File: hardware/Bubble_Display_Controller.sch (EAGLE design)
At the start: 37 parts, among them J1 ICSP, Q1 BSS84, Q10 BSS123, Q11 BSS123, Q12 BSS123, Q13 BSS123, Q14 BSS123, Q15 BSS123, Q16 BSS123, Q2 BSS84, Q3 BSS84, Q4 BSS84, Q5 BSS84, Q6 BSS84, Q7 BSS84, Q8 BSS84, Q9 BSS123, U4 ATMEGA328, Y1 16MHz

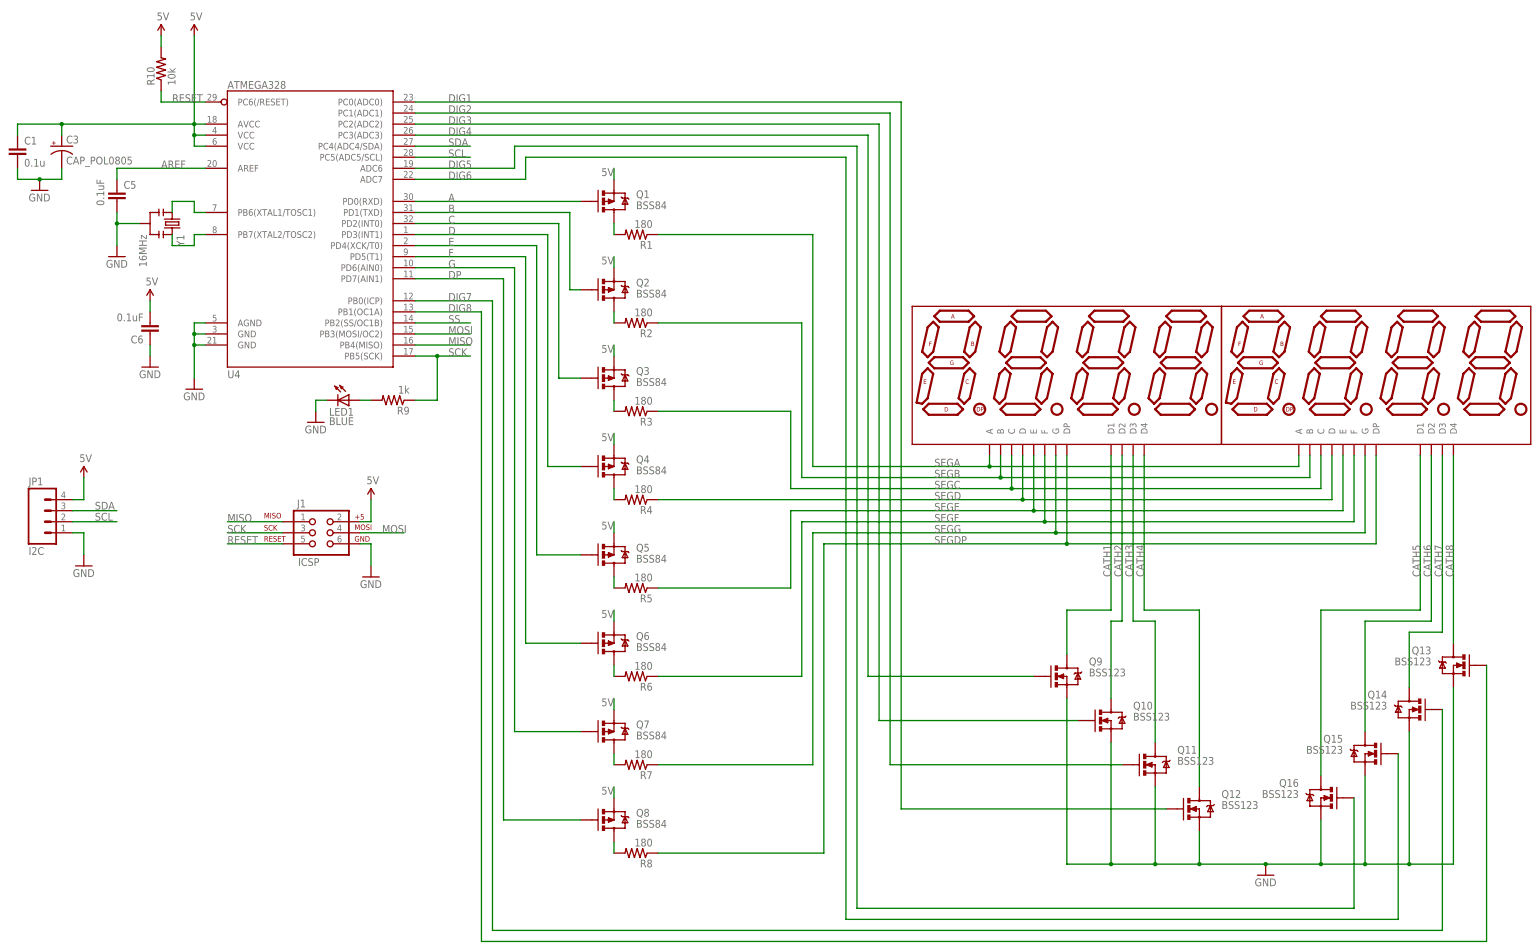
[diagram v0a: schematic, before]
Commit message: Updating comp values per simulation. Added BOM. Started firmware.
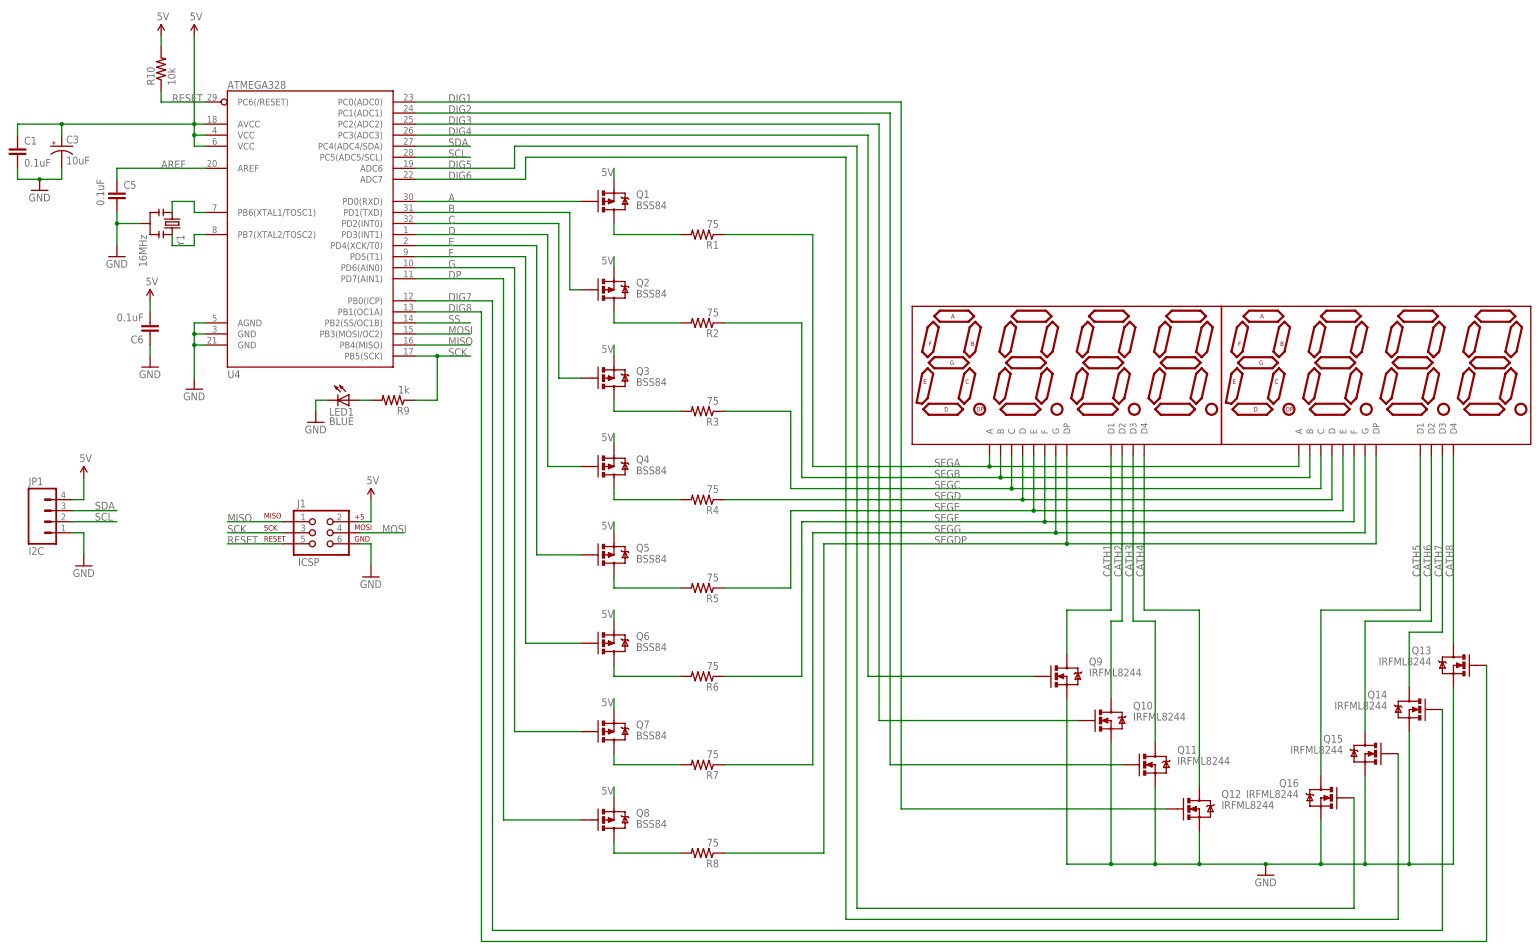
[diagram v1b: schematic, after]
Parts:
- C1: value 0.1u -> 0.1uF
- C3: value CAP_POL0805 -> 10uF
- Q10, Q11, Q12, Q13, Q14, Q15, Q16, Q9: value BSS123 -> IRFML8244
- R1, R2, R3, R4, R5, R6, R7, R8: value 180 -> 75
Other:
- moved on the sheet: R1, R2, R3, R4, R5, R6, R7, R8

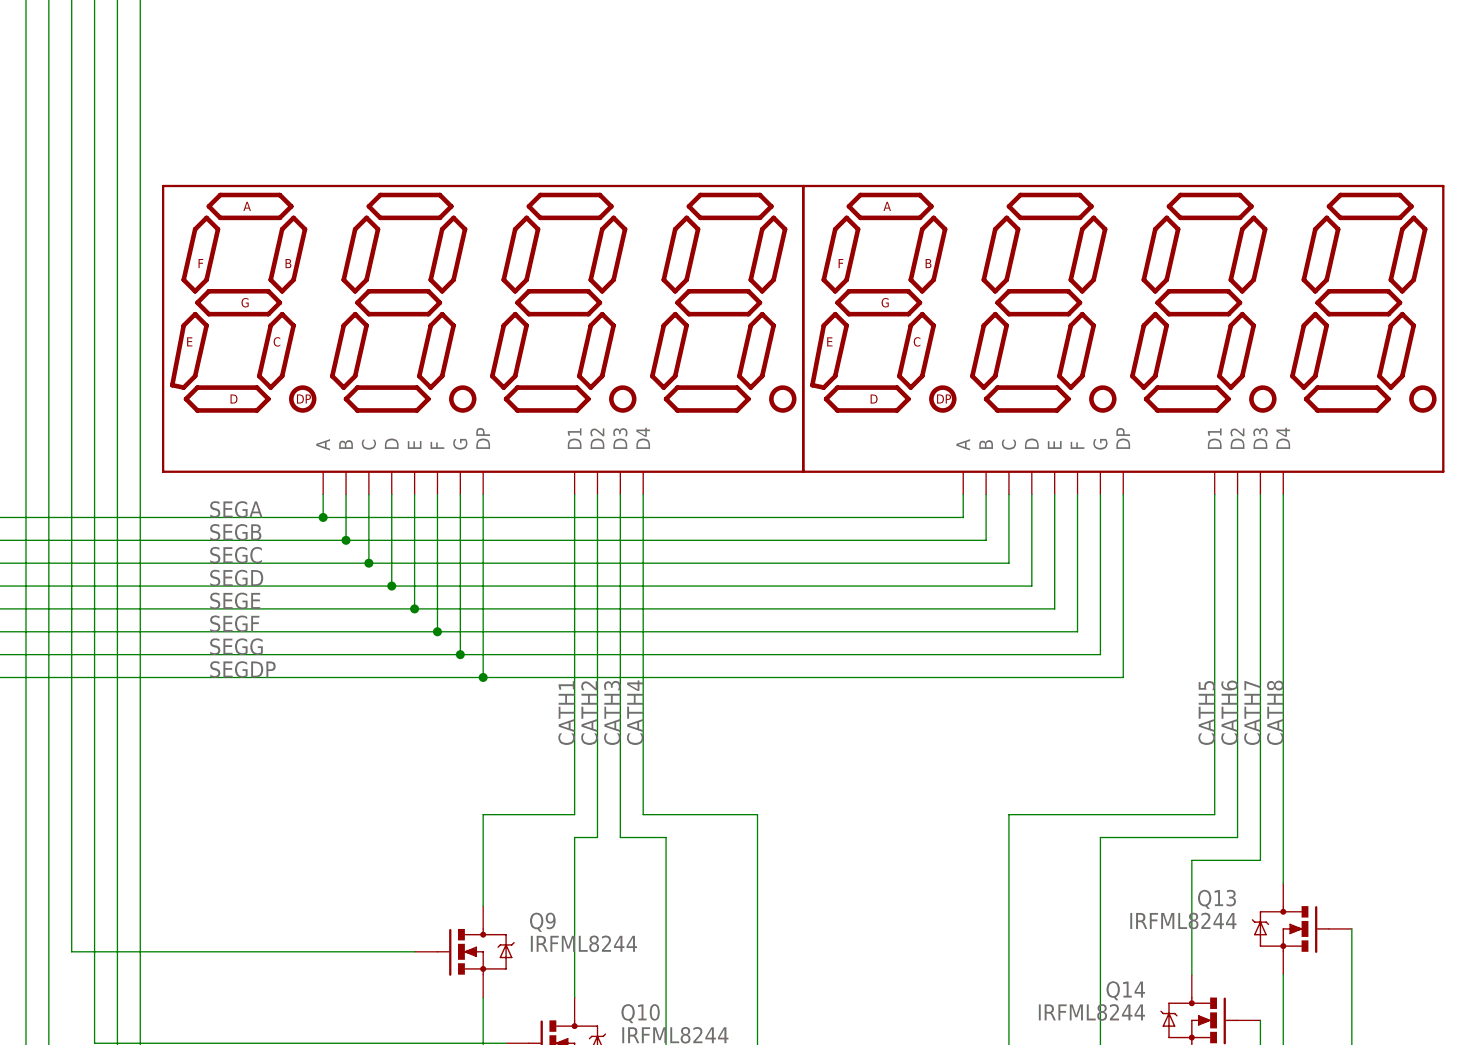
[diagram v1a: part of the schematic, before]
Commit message: Updated to use new HP Display component in my fork of SparkFun libraries
Also worked on CharGenROM.h; converted segments to HP config.  Added
proper port manipulation to Display_Firmware.ino.
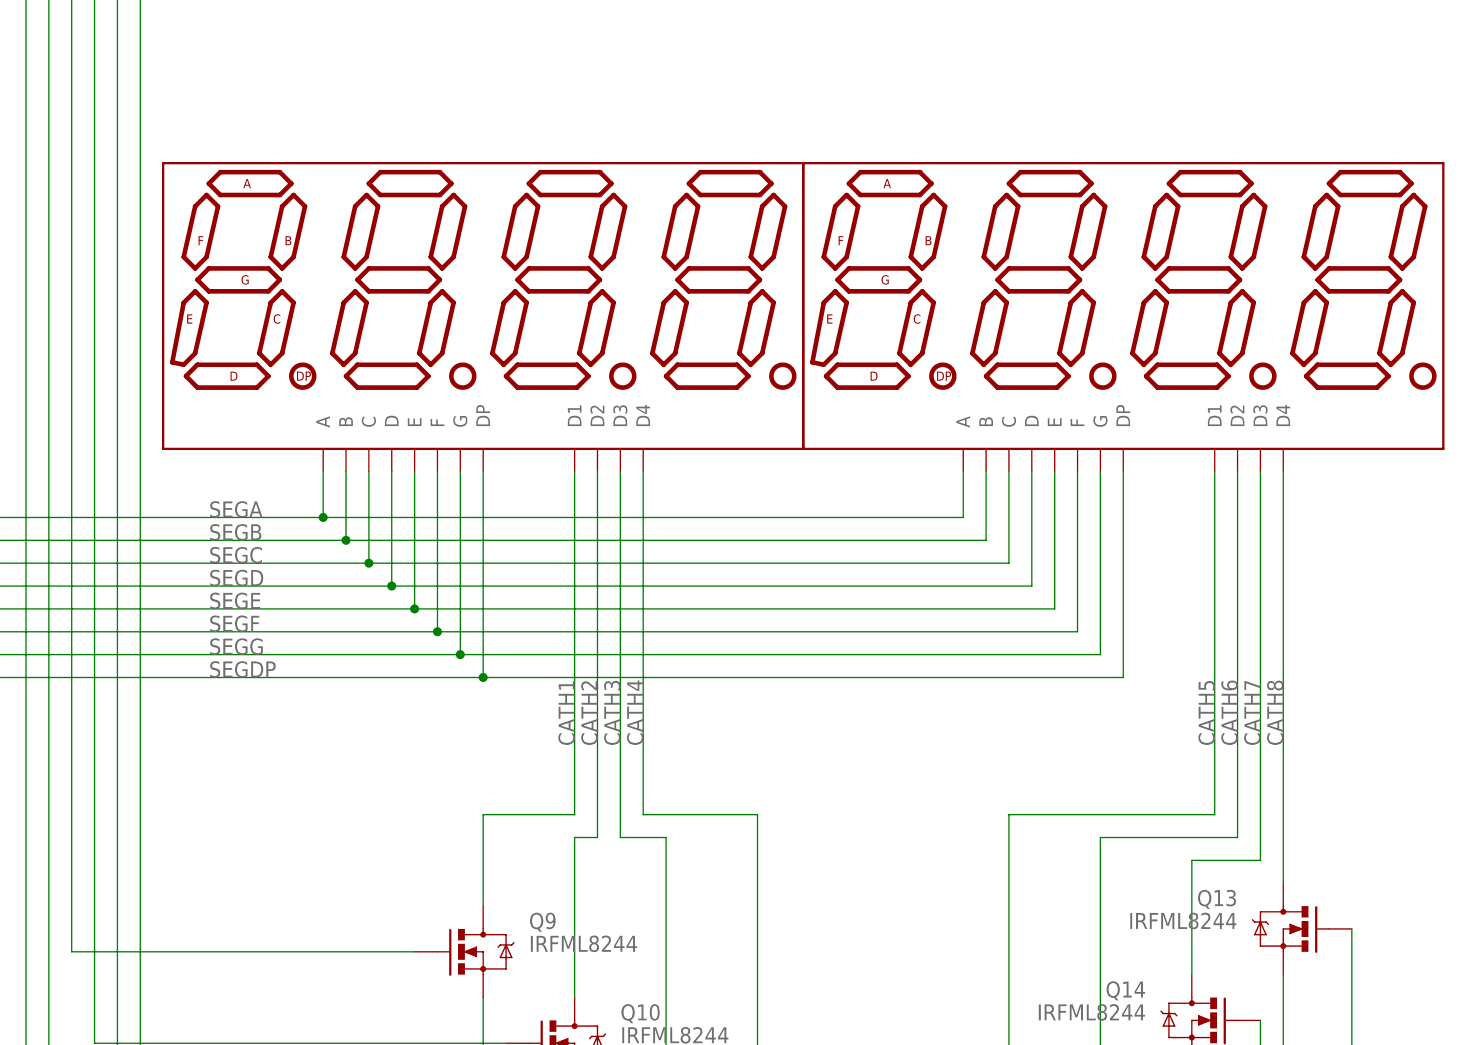
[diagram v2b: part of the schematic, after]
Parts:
- DISPLAY1, DISPLAY2: device SparkFun-Displays:7-SEGMENT-4DIGIT-COUNTER-HP-BUBBLE-DISPLAY -> SparkFun-Displays:7-SEGMENT-4DIGIT-COUNTER-HP-BUBBLE
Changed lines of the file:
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@@
 </classes>
 <parts>
-<part name="DISPLAY1" library="SparkFun-Displays" deviceset="7-SEGMENT-4DIGIT-COUNTER" device="-HP-BUBBLE-DISPLAY" value="hp"/>
-<part name="DISPLAY2" library="SparkFun-Displays" deviceset="7-SEGMENT-4DIGIT-COUNTER" device="-HP-BUBBLE-DISPLAY" value="hp"/>
+<part name="DISPLAY1" library="SparkFun-Displays" deviceset="7-SEGMENT-4DIGIT-COUNTER" device="-HP-BUBBLE" value="hp"/>
+<part name="DISPLAY2" library="SparkFun-Displays" deviceset="7-SEGMENT-4DIGIT-COUNTER" device="-HP-BUBBLE" value="hp"/>
 <part name="Q1" library="SparkFun-DiscreteSemi" deviceset="MOSFET-PCHANNEL" device="SMD" value="BSS84"/>
 <part name="R1" library="SparkFun-Resistors" deviceset="RESISTOR" device="0805-RES" value="75"/>
@@
 </plain>
 <instances>
-<instance part="DISPLAY1" gate="G$1" x="-25.4" y="0"/>
-<instance part="DISPLAY2" gate="G$1" x="45.72" y="0"/>
+<instance part="DISPLAY1" gate="G$1" x="-25.4" y="2.54"/>
+<instance part="DISPLAY2" gate="G$1" x="45.72" y="2.54"/>
 <instance part="Q1" gate="G$1" x="-129.54" y="40.64" smashed="yes" rot="MR180">
 <attribute name="NAME" x="-124.46" y="43.18" size="1.778" layer="95" rot="MR180"/>
@@
 <segment>
 <pinref part="DISPLAY2" gate="G$1" pin="B"/>
-<wire x1="30.48" y1="-17.78" x2="30.48" y2="-22.86" width="0.1524" layer="91"/>
+<wire x1="30.48" y1="-15.24" x2="30.48" y2="-22.86" width="0.1524" layer="91"/>
 <wire x1="30.48" y1="-22.86" x2="-40.64" y2="-22.86" width="0.1524" layer="91"/>
 <pinref part="DISPLAY1" gate="G$1" pin="B"/>
-<wire x1="-40.64" y1="-22.86" x2="-40.64" y2="-17.78" width="0.1524" layer="91"/>
+<wire x1="-40.64" y1="-22.86" x2="-40.64" y2="-15.24" width="0.1524" layer="91"/>
 <wire x1="-40.64" y1="-22.86" x2="-86.36" y2="-22.86" width="0.1524" layer="91"/>
 <wire x1="-86.36" y1="-22.86" x2="-86.36" y2="12.7" width="0.1524" layer="91"/>
@@
 <segment>
 <pinref part="DISPLAY2" gate="G$1" pin="D"/>
-<wire x1="35.56" y1="-17.78" x2="35.56" y2="-27.94" width="0.1524" layer="91"/>
+<wire x1="35.56" y1="-15.24" x2="35.56" y2="-27.94" width="0.1524" layer="91"/>
 <wire x1="35.56" y1="-27.94" x2="-35.56" y2="-27.94" width="0.1524" layer="91"/>
 <pinref part="DISPLAY1" gate="G$1" pin="D"/>
-<wire x1="-35.56" y1="-27.94" x2="-35.56" y2="-17.78" width="0.1524" layer="91"/>
+<wire x1="-35.56" y1="-27.94" x2="-35.56" y2="-15.24" width="0.1524" layer="91"/>
 <wire x1="-35.56" y1="-27.94" x2="-104.14" y2="-27.94" width="0.1524" layer="91"/>
 <pinref part="R4" gate="G$1" pin="1"/>
@@
 <segment>
 <pinref part="DISPLAY2" gate="G$1" pin="E"/>
-<wire x1="38.1" y1="-17.78" x2="38.1" y2="-30.48" width="0.1524" layer="91"/>
+<wire x1="38.1" y1="-15.24" x2="38.1" y2="-30.48" width="0.1524" layer="91"/>
 <wire x1="38.1" y1="-30.48" x2="-33.02" y2="-30.48" width="0.1524" layer="91"/>
 <pinref part="DISPLAY1" gate="G$1" pin="E"/>
-<wire x1="-33.02" y1="-30.48" x2="-33.02" y2="-17.78" width="0.1524" layer="91"/>
+<wire x1="-33.02" y1="-30.48" x2="-33.02" y2="-15.24" width="0.1524" layer="91"/>
 <pinref part="R5" gate="G$1" pin="1"/>
 <wire x1="-88.9" y1="-48.26" x2="-104.14" y2="-48.26" width="0.1524" layer="91"/>
@@
 <segment>
 <pinref part="DISPLAY2" gate="G$1" pin="F"/>
-<wire x1="40.64" y1="-17.78" x2="40.64" y2="-33.02" width="0.1524" layer="91"/>
+<wire x1="40.64" y1="-15.24" x2="40.64" y2="-33.02" width="0.1524" layer="91"/>
 <wire x1="40.64" y1="-33.02" x2="-30.48" y2="-33.02" width="0.1524" layer="91"/>
 <pinref part="DISPLAY1" gate="G$1" pin="F"/>
-<wire x1="-30.48" y1="-33.02" x2="-30.48" y2="-17.78" width="0.1524" layer="91"/>
+<wire x1="-30.48" y1="-33.02" x2="-30.48" y2="-15.24" width="0.1524" layer="91"/>
 <wire x1="-86.36" y1="-68.58" x2="-104.14" y2="-68.58" width="0.1524" layer="91"/>
 <pinref part="R6" gate="G$1" pin="1"/>
@@
 <segment>
 <pinref part="DISPLAY2" gate="G$1" pin="G"/>
-<wire x1="43.18" y1="-17.78" x2="43.18" y2="-35.56" width="0.1524" layer="91"/>
+<wire x1="43.18" y1="-15.24" x2="43.18" y2="-35.56" width="0.1524" layer="91"/>
 <wire x1="43.18" y1="-35.56" x2="-27.94" y2="-35.56" width="0.1524" layer="91"/>
 <pinref part="DISPLAY1" gate="G$1" pin="G"/>
-<wire x1="-27.94" y1="-35.56" x2="-27.94" y2="-17.78" width="0.1524" layer="91"/>
+<wire x1="-27.94" y1="-35.56" x2="-27.94" y2="-15.24" width="0.1524" layer="91"/>
 <wire x1="-27.94" y1="-35.56" x2="-83.82" y2="-35.56" width="0.1524" layer="91"/>
 <wire x1="-83.82" y1="-35.56" x2="-83.82" y2="-88.9" width="0.1524" layer="91"/>
@@
 <segment>
 <pinref part="DISPLAY2" gate="G$1" pin="DP"/>
-<wire x1="45.72" y1="-17.78" x2="45.72" y2="-38.1" width="0.1524" layer="91"/>
+<wire x1="45.72" y1="-15.24" x2="45.72" y2="-38.1" width="0.1524" layer="91"/>
 <wire x1="45.72" y1="-38.1" x2="-25.4" y2="-38.1" width="0.1524" layer="91"/>
 <pinref part="DISPLAY1" gate="G$1" pin="DP"/>
-<wire x1="-25.4" y1="-38.1" x2="-25.4" y2="-17.78" width="0.1524" layer="91"/>
+<wire x1="-25.4" y1="-38.1" x2="-25.4" y2="-15.24" width="0.1524" layer="91"/>
 <pinref part="R8" gate="G$1" pin="1"/>
 <wire x1="-81.28" y1="-109.22" x2="-104.14" y2="-109.22" width="0.1524" layer="91"/>
@@
 <segment>
 <pinref part="DISPLAY1" gate="G$1" pin="D4"/>
-<wire x1="-7.62" y1="-53.34" x2="-7.62" y2="-17.78" width="0.1524" layer="91"/>
+<wire x1="-7.62" y1="-53.34" x2="-7.62" y2="-15.24" width="0.1524" layer="91"/>
 <label x="-7.62" y="-45.72" size="1.778" layer="95" rot="R90"/>
 <wire x1="5.08" y1="-93.98" x2="5.08" y2="-53.34" width="0.1524" layer="91"/>
@@
 <segment>
 <pinref part="DISPLAY2" gate="G$1" pin="D4"/>
-<wire x1="63.5" y1="-60.96" x2="63.5" y2="-17.78" width="0.1524" layer="91"/>
+<wire x1="63.5" y1="-60.96" x2="63.5" y2="-15.24" width="0.1524" layer="91"/>
 <label x="63.5" y="-45.72" size="1.778" layer="95" rot="R90"/>
 <pinref part="Q13" gate="G$1" pin="D"/>
@@
 <wire x1="-83.82" y1="33.02" x2="-83.82" y2="-20.32" width="0.1524" layer="91"/>
 <pinref part="DISPLAY2" gate="G$1" pin="A"/>
-<wire x1="27.94" y1="-17.78" x2="27.94" y2="-20.32" width="0.1524" layer="91"/>
+<wire x1="27.94" y1="-15.24" x2="27.94" y2="-20.32" width="0.1524" layer="91"/>
 <wire x1="27.94" y1="-20.32" x2="-43.18" y2="-20.32" width="0.1524" layer="91"/>
 <pinref part="DISPLAY1" gate="G$1" pin="A"/>
-<wire x1="-43.18" y1="-20.32" x2="-43.18" y2="-17.78" width="0.1524" layer="91"/>
 <wire x1="-83.82" y1="-20.32" x2="-43.18" y2="-20.32" width="0.1524" layer="91"/>
+<wire x1="-43.18" y1="-20.32" x2="-43.18" y2="-15.24" width="0.1524" layer="91"/>
+<label x="-55.88" y="-20.32" size="1.778" layer="95"/>
 <junction x="-43.18" y="-20.32"/>
-<label x="-55.88" y="-20.32" size="1.778" layer="95"/>
 </segment>
 </net>
@@
 <wire x1="-88.9" y1="-7.62" x2="-88.9" y2="-25.4" width="0.1524" layer="91"/>
 <pinref part="DISPLAY2" gate="G$1" pin="C"/>
-<wire x1="33.02" y1="-17.78" x2="33.02" y2="-25.4" width="0.1524" layer="91"/>
+<wire x1="33.02" y1="-15.24" x2="33.02" y2="-25.4" width="0.1524" layer="91"/>
 <wire x1="33.02" y1="-25.4" x2="-38.1" y2="-25.4" width="0.1524" layer="91"/>
 <pinref part="DISPLAY1" gate="G$1" pin="C"/>
-<wire x1="-38.1" y1="-25.4" x2="-38.1" y2="-17.78" width="0.1524" layer="91"/>
+<wire x1="-38.1" y1="-25.4" x2="-38.1" y2="-15.24" width="0.1524" layer="91"/>
 <wire x1="-88.9" y1="-25.4" x2="-38.1" y2="-25.4" width="0.1524" layer="91"/>
 <junction x="-38.1" y="-25.4"/>
@@
 <segment>
 <pinref part="DISPLAY1" gate="G$1" pin="D3"/>
-<wire x1="-10.16" y1="-17.78" x2="-10.16" y2="-55.88" width="0.1524" layer="91"/>
+<wire x1="-10.16" y1="-15.24" x2="-10.16" y2="-55.88" width="0.1524" layer="91"/>
 <wire x1="-10.16" y1="-55.88" x2="-5.08" y2="-55.88" width="0.1524" layer="91"/>
 <wire x1="-5.08" y1="-55.88" x2="-5.08" y2="-83.82" width="0.1524" layer="91"/>
@@
 <segment>
 <pinref part="DISPLAY1" gate="G$1" pin="D2"/>
-<wire x1="-12.7" y1="-17.78" x2="-12.7" y2="-55.88" width="0.1524" layer="91"/>
+<wire x1="-12.7" y1="-15.24" x2="-12.7" y2="-55.88" width="0.1524" layer="91"/>
 <wire x1="-12.7" y1="-55.88" x2="-15.24" y2="-55.88" width="0.1524" layer="91"/>
 <wire x1="-15.24" y1="-55.88" x2="-15.24" y2="-73.66" width="0.1524" layer="91"/>
@@
 <segment>
 <pinref part="DISPLAY1" gate="G$1" pin="D1"/>
-<wire x1="-15.24" y1="-17.78" x2="-15.24" y2="-53.34" width="0.1524" layer="91"/>
+<wire x1="-15.24" y1="-15.24" x2="-15.24" y2="-53.34" width="0.1524" layer="91"/>
 <wire x1="-15.24" y1="-53.34" x2="-25.4" y2="-53.34" width="0.1524" layer="91"/>
 <wire x1="-25.4" y1="-53.34" x2="-25.4" y2="-63.5" width="0.1524" layer="91"/>
@@
 <segment>
 <pinref part="DISPLAY2" gate="G$1" pin="D1"/>
-<wire x1="55.88" y1="-17.78" x2="55.88" y2="-53.34" width="0.1524" layer="91"/>
+<wire x1="55.88" y1="-15.24" x2="55.88" y2="-53.34" width="0.1524" layer="91"/>
 <wire x1="55.88" y1="-53.34" x2="33.02" y2="-53.34" width="0.1524" layer="91"/>
 <wire x1="33.02" y1="-53.34" x2="33.02" y2="-91.44" width="0.1524" layer="91"/>
@@
 <segment>
 <pinref part="DISPLAY2" gate="G$1" pin="D2"/>
-<wire x1="58.42" y1="-17.78" x2="58.42" y2="-55.88" width="0.1524" layer="91"/>
+<wire x1="58.42" y1="-15.24" x2="58.42" y2="-55.88" width="0.1524" layer="91"/>
 <wire x1="58.42" y1="-55.88" x2="43.18" y2="-55.88" width="0.1524" layer="91"/>
 <wire x1="43.18" y1="-55.88" x2="43.18" y2="-81.28" width="0.1524" layer="91"/>
@@
 <segment>
 <pinref part="DISPLAY2" gate="G$1" pin="D3"/>
-<wire x1="60.96" y1="-17.78" x2="60.96" y2="-58.42" width="0.1524" layer="91"/>
+<wire x1="60.96" y1="-15.24" x2="60.96" y2="-58.42" width="0.1524" layer="91"/>
 <wire x1="60.96" y1="-58.42" x2="53.34" y2="-58.42" width="0.1524" layer="91"/>
 <wire x1="53.34" y1="-58.42" x2="53.34" y2="-71.12" width="0.1524" layer="91"/>
